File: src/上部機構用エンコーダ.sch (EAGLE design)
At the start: 14 parts

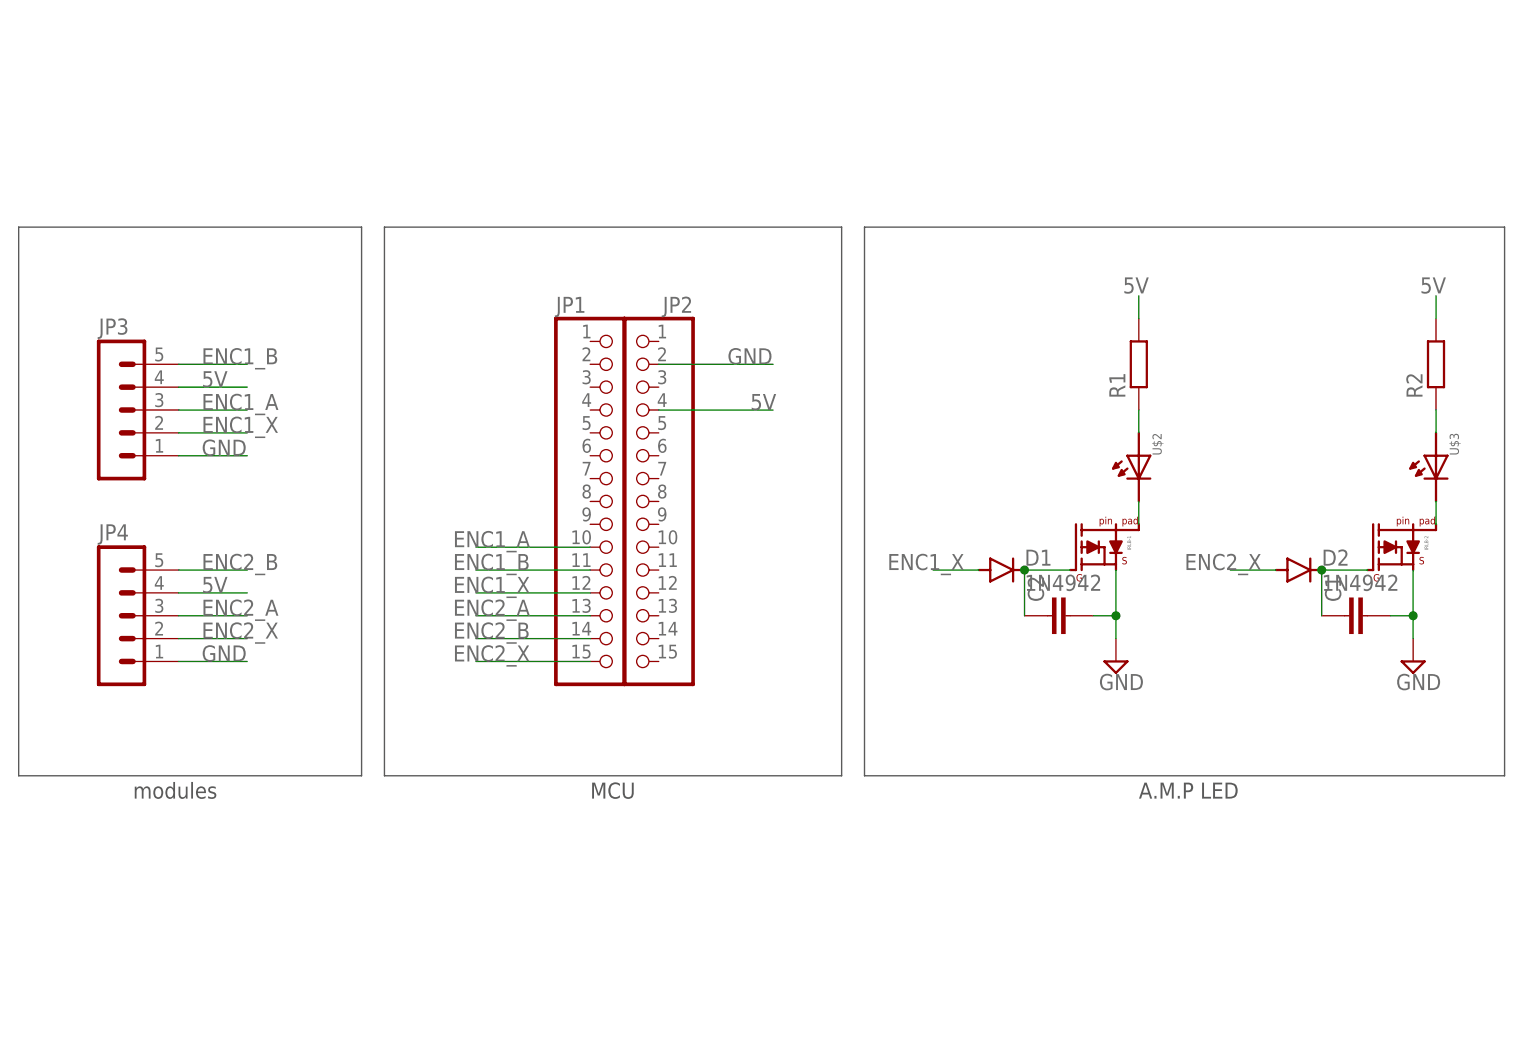
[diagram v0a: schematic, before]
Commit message: 上部機構用エンコーダー 回路の微修正
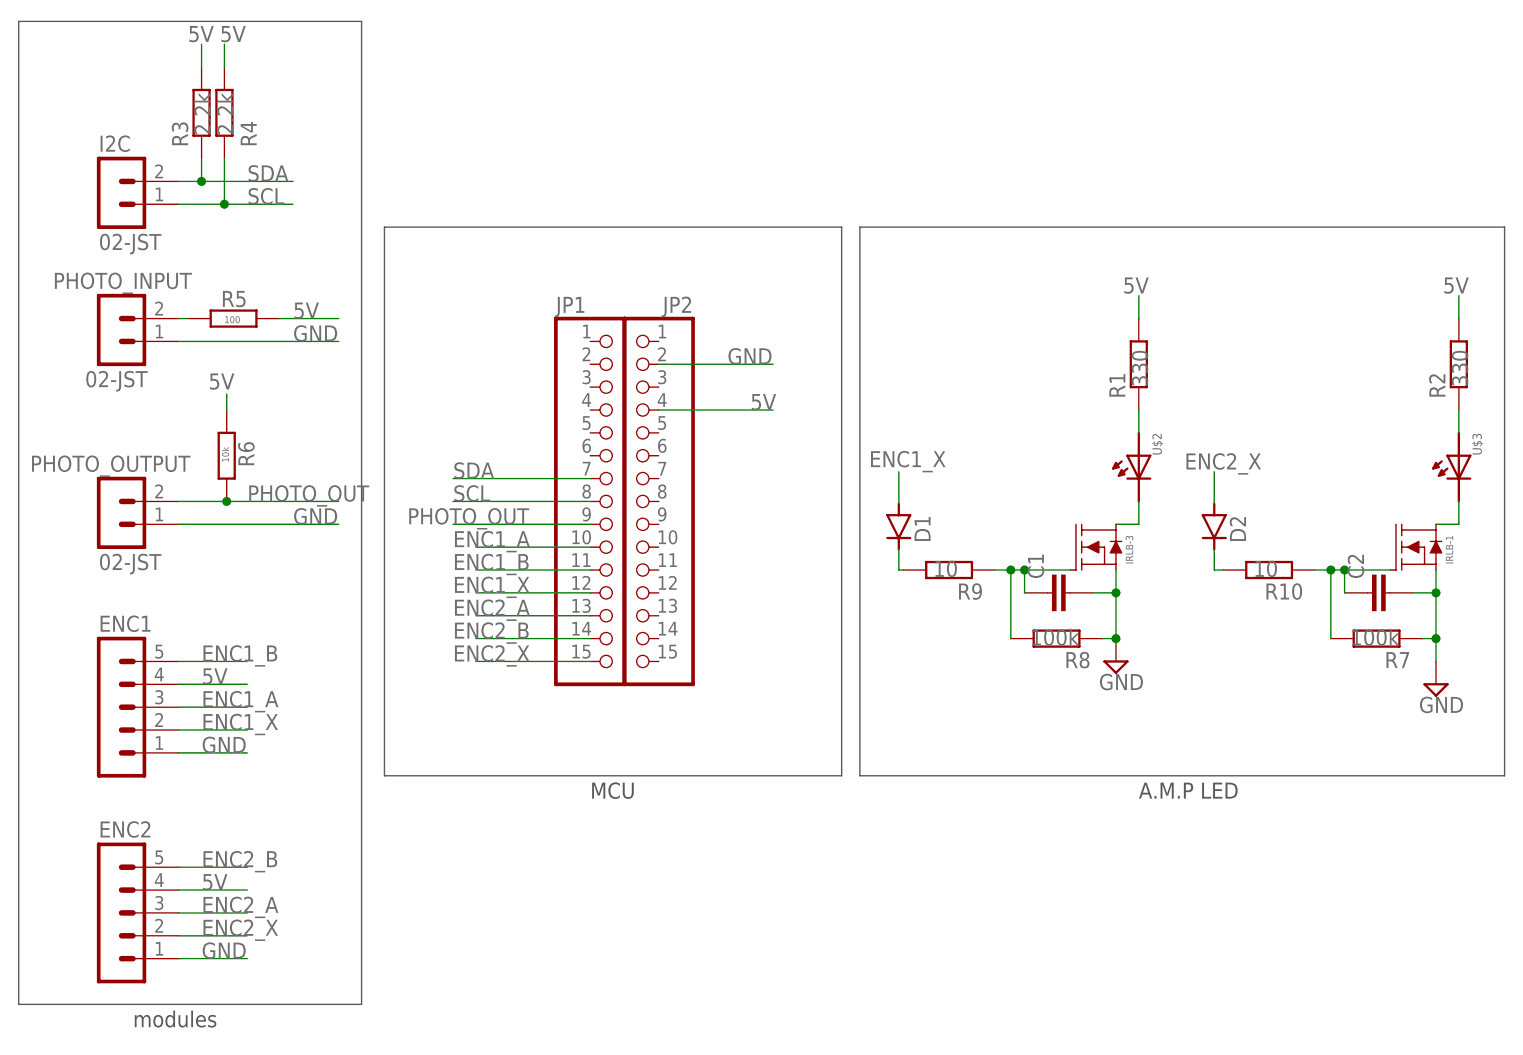
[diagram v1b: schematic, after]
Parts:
- removed IRLB-2: IRLB3813_2, OKUDA_libraries:IRLB3813_2
- removed JP3, JP4: (no value), con-jst-xh:05-JST
- added ENC1, ENC2: (no value), con-jst-xh:05-JST
- added I2C, PHOTO_INPUT, PHOTO_OUTPUT: 02-JST, con-jst-xh:02-JST
- added IRLB-3: IRLB3813STAND, OKUDA_libraries:IRLB3813STAND
- added R10, R9: 10, rcl:R-EU_0207/2V
- added R3, R4: 2.2k, rcl:R-EU_0207/2V
- added R5: 100, rcl:R-EU_0204/7
- added R6: 10k, rcl:R-EU_0204/7
- added R7, R8: 100k, rcl:R-EU_0207/2V
- C1, C2: device capacitor-wima:C2.5/2 -> capacitor-wima:C5/2.5
- D1, D2: value 1N4942 -> DIODE_STAND; device diode:1N4942 -> DIODE_STAND:DIODE_STAND
- IRLB-1: value IRLB3813_2 -> IRLB3813STAND; device OKUDA_libraries:IRLB3813_2 -> OKUDA_libraries:IRLB3813STAND
- R1, R2: value (none) -> 330; device rcl:R-EU_0204/7 -> rcl:R-EU_0207/2V
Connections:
- new net N$7: PHOTO_INPUT.2, R5.2
- new net N$8: D1.C, R9.2
- new net N$9: D2.C, R10.2
- new net PHOTO_OUT: JP1.9, PHOTO_OUTPUT.2, R6.1
- new net SCL: I2C.1, JP1.8, R4.1
- new net SDA: I2C.2, JP1.7, R3.1
- net 5V: now also ENC1.4, ENC2.4, R3.2, R4.2, R5.1, R6.2; no longer JP3.4, JP4.4
- net ENC1_A: now also ENC1.3; no longer JP3.3
- net ENC1_B: now also ENC1.5; no longer JP3.5
- net ENC1_X: now also ENC1.2; no longer JP3.2
- net ENC2_A: now also ENC2.3; no longer JP4.3
- net ENC2_B: now also ENC2.5; no longer JP4.5
- net ENC2_X: now also ENC2.2; no longer JP4.2
- net GND: now also ENC1.1, ENC2.1, IRLB-3.S, PHOTO_INPUT.1, PHOTO_OUTPUT.1, R7.1, R8.1; no longer IRLB-2.S, JP3.1, JP4.1
- net N$1: now also IRLB-3.D; no longer IRLB-1.PD
- net N$3: now also C1.1, IRLB-3.G, R8.2, R9.1; no longer C2.1, D1.C, IRLB-1.G
- net N$4: now also C2.1, IRLB-1.G, R10.1, R7.2; no longer C1.1, D2.C, IRLB-2.G
- net N$5: now also IRLB-1.D; no longer IRLB-2.PD
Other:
- moved on the sheet: C1, C2, R2, U$3
